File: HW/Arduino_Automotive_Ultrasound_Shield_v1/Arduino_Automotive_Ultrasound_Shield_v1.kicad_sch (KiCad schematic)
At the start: 9 parts, among them J1 Conn_01x04_Socket, J2 Conn_01x04_Socket, J3 Barrel_Jack_Switch, J4 Conn_01x04_Socket, J5 1x3 2.54mm male, J6 1x3 2.54mm male, SW1 SW_Push, U2 LM7805_TO220

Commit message: pcb
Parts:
- removed J4: Conn_01x04_Socket, Connector_PinSocket_2.54mm:PinSocket_1x04_P2.54mm_Vertical, symbol Connector:Conn_01x04_Socket
- added H1, H2, H3, H4: M3, MountingHole:MountingHole_3.2mm_M3, symbol Mechanical:MountingHole
- added J7: 1x4 2.54mm female, Connector_PinSocket_2.54mm:PinSocket_1x04_P2.54mm_Vertical, symbol Connector:Conn_01x04_Socket
- added SW2, SW3, SW4: SW_Push, Button_Switch_THT:SW_PUSH_6mm, symbol Switch:SW_Push
- J1, J2: value Conn_01x04_Socket -> 1x4 2.54mm female
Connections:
- net +5V: now also J1.4 (Pin_4), J2.4 (Pin_4), J7.4 (Pin_4); no longer J1.Vcc (Pin_4), J2.Vcc (Pin_4)
- net ECHO_0: now also A2.26 (A7), J7.2 (Pin_2); no longer A2.19 (A0), J2.Echo (Pin_2)
- net ECHO_1: now also A2.24 (SCL/A5), J2.2 (Pin_2)
- net ECHO_2: now also A2.10 (D7), J1.2 (Pin_2); no longer A2.21 (A2), J1.Echo (Pin_2)
- net GND: now also J1.1 (Pin_1), J2.1 (Pin_1), SW1.2, J7.1 (Pin_1), SW2.2, SW3.2, SW4.2; no longer J1.GND (Pin_1), J2.GND (Pin_1)
- net TRIG_0: now also A2.25 (A6), J7.3 (Pin_3); no longer A2.20 (A1), J2.Trig (Pin_3)
- net TRIG_1: now also A2.23 (SDA/A4), J2.3 (Pin_3)
- net TRIG_2: now also A2.9 (D6), J1.3 (Pin_3); no longer A2.22 (A3), J1.Trig (Pin_3)
- net PB0: now reaches SW1.1
- net PB0: now also A2.19 (A0)
- net PB3: now reaches A2.16 (SCK)
- net PB3: now also SW4.1
- new net PB1: A2.20 (A1), SW2.1
- new net PB2: A2.21 (A2), SW3.1
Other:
- moved on the sheet: SW1

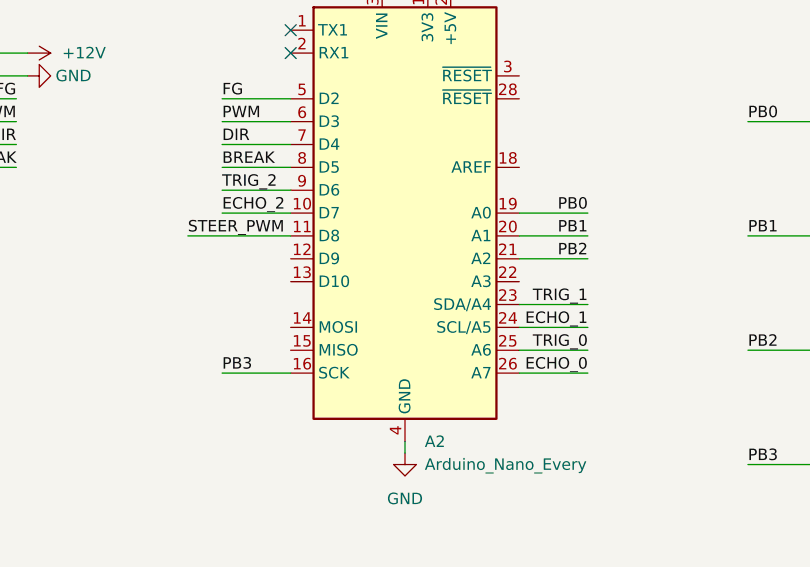
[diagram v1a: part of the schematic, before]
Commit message: promenjen pin
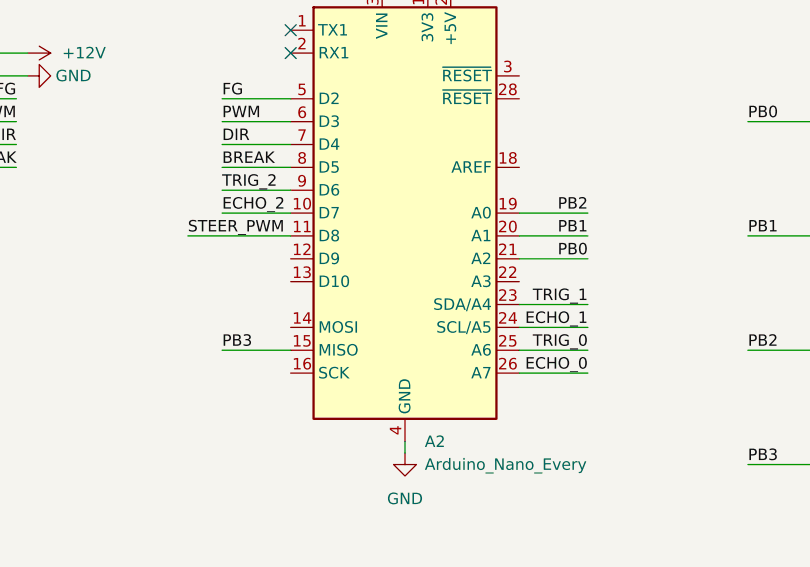
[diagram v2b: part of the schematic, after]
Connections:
- net PB0: now also A2.21 (A2); no longer A2.19 (A0)
- net PB2: now also A2.19 (A0); no longer A2.21 (A2)
- net PB3: now also A2.15 (MISO); no longer A2.16 (SCK)
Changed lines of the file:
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@@
 	(wire
 		(pts
-			(xy 152.4 109.22) (xy 160.02 109.22)
+			(xy 152.4 106.68) (xy 160.02 106.68)
 		)
 		(stroke
@@
 		)
 	)
-	(label "PB0"
+	(label "PB2"
 		(at 193.04 91.44 180)
 		(effects
@@
 		)
 	)
-	(label "PB2"
+	(label "PB0"
 		(at 193.04 96.52 180)
 		(effects
@@
 	)
 	(label "PB3"
-		(at 152.4 109.22 0)
-		(effects
-			(font
+		(at 152.4 106.68 0)
+		(effects
+			(font
